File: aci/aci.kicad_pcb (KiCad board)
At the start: 2 copper layers, 102.2 x 53.3 mm, 0 parts

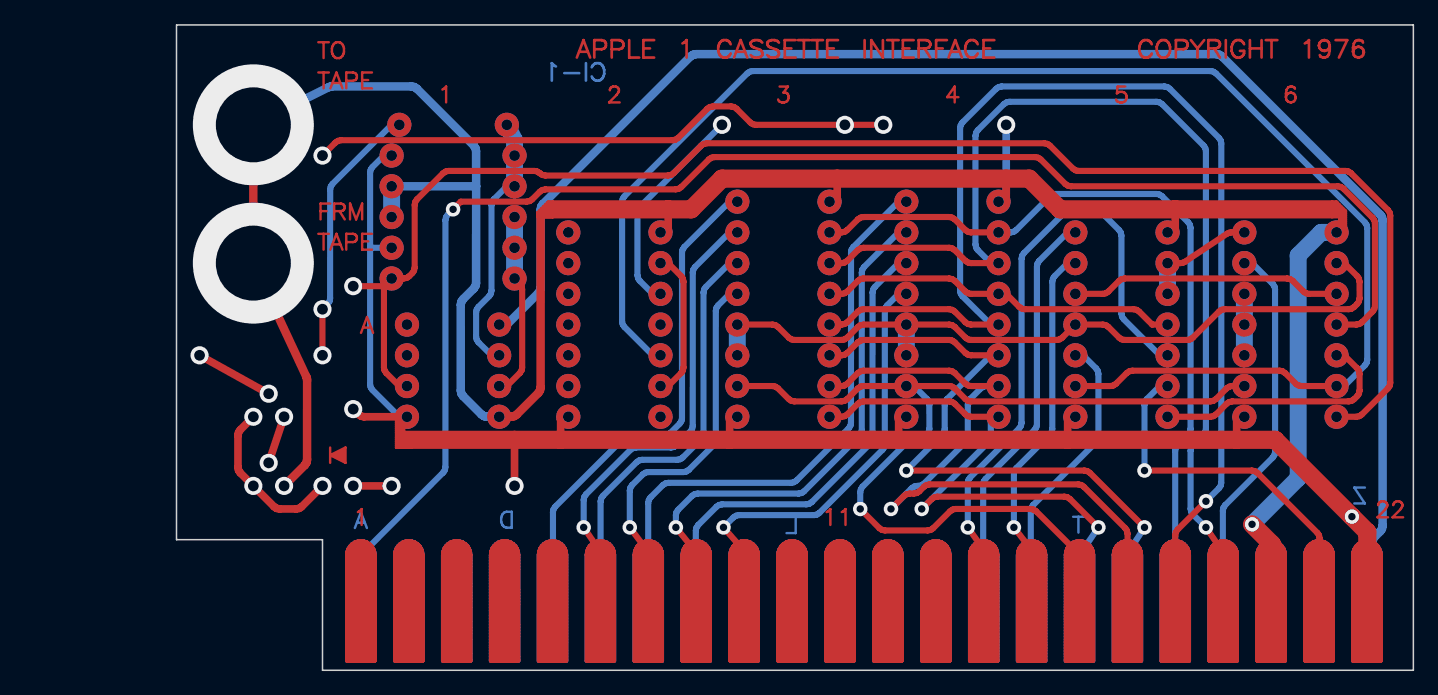
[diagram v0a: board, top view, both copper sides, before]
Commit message: new file:   aci/README.md modified:   aci/aci.kicad_pcb new file:   aci/aci.kicad_pro modified:   aci/aci.kicad_sch deleted:    aci/aci.pro deleted:    aci/aci.sch new file:   doc/apple1cassette.pdf deleted:    doc/progress3d.png
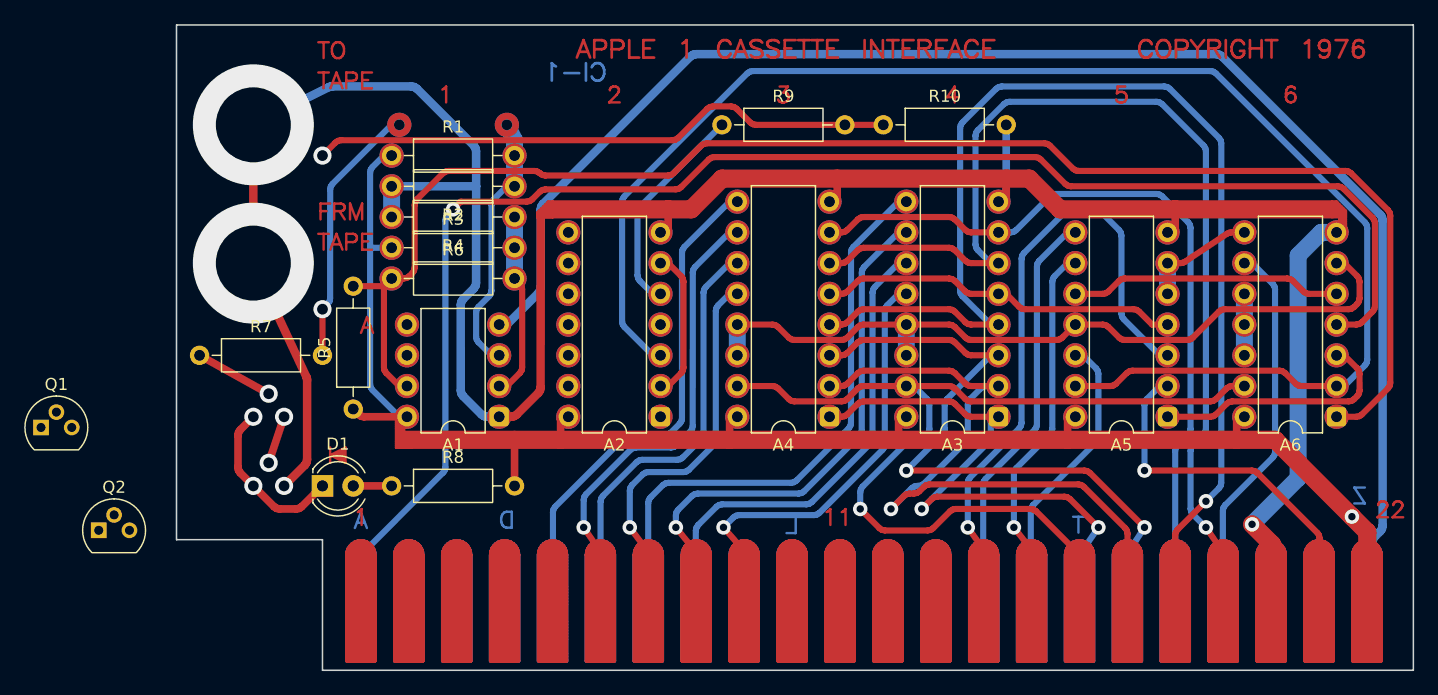
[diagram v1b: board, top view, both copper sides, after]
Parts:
- added A1: LM311, Package_DIP:DIP-8_W7.62mm, F.Cu at (36.8, -31.1)
- added A2: 74LS74, Package_DIP:DIP-14_W7.62mm, F.Cu at (50.2, -31.1)
- added A3: 82S129, Package_DIP:DIP-16_W7.62mm, F.Cu at (78.1, -31.1)
- added A4: 82S129, Package_DIP:DIP-16_W7.62mm, F.Cu at (64.1, -31.1)
- added A5: 74LS02, Package_DIP:DIP-14_W7.62mm, F.Cu at (92.1, -31.1)
- added A6: 74LS10, Package_DIP:DIP-14_W7.62mm, F.Cu at (106.0, -31.1)
- added D1: LED_Small_ALT, LED_THT:LED_D4.0mm, F.Cu at (22.2, -25.4)
- added Q1: Q_NPN_EBC, Package_TO_SOT_THT:TO-92, F.Cu at (-1.04, -30.2)
- added Q2: Q_NPN_EBC, Package_TO_SOT_THT:TO-92, F.Cu at (3.73, -21.7)
- added R1: 10k, Resistor_THT:R_Axial_DIN0207_L6.3mm_D2.5mm_P10.16mm_Horizontal, F.Cu at (27.9, -52.7)
- added R10: 100, Resistor_THT:R_Axial_DIN0207_L6.3mm_D2.5mm_P10.16mm_Horizontal, F.Cu at (68.6, -55.2)
- added R2: 10k, Resistor_THT:R_Axial_DIN0207_L6.3mm_D2.5mm_P10.16mm_Horizontal, F.Cu at (38.1, -50.2)
- added R3: 10k, Resistor_THT:R_Axial_DIN0207_L6.3mm_D2.5mm_P10.16mm_Horizontal, F.Cu at (27.9, -45.1)
- added R4: 10k, Resistor_THT:R_Axial_DIN0207_L6.3mm_D2.5mm_P10.16mm_Horizontal, F.Cu at (38.1, -47.6)
- added R5: 3k, Resistor_THT:R_Axial_DIN0207_L6.3mm_D2.5mm_P10.16mm_Horizontal, F.Cu at (24.8, -31.8)
- added R6: 47k, Resistor_THT:R_Axial_DIN0207_L6.3mm_D2.5mm_P10.16mm_Horizontal, F.Cu at (27.9, -42.5)
- added R7: 100k, Resistor_THT:R_Axial_DIN0207_L6.3mm_D2.5mm_P10.16mm_Horizontal, F.Cu at (12.1, -36.2)
- added R8: 100, Resistor_THT:R_Axial_DIN0207_L6.3mm_D2.5mm_P10.16mm_Horizontal, F.Cu at (27.9, -25.4)
- added R9: 10k, Resistor_THT:R_Axial_DIN0207_L6.3mm_D2.5mm_P10.16mm_Horizontal, F.Cu at (55.2, -55.2)
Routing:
- net 0: track 11525.1 -> 0.00 mm
- net (no net): track 0.00 -> 4125.1 mm, vias 134 -> 8
- net GND: track 0.00 -> 458.4 mm, vias 0 -> 13
- net +5V: track 0.00 -> 362.7 mm, vias 0 -> 11
- net Net-(J3A-ɸ2): track 0.00 -> 332.7 mm, vias 0 -> 2
- net -12V: track 0.00 -> 330.3 mm, vias 0 -> 1
- net Net-(A3-A3): track 0.00 -> 303.6 mm, vias 0 -> 3
- net Net-(A3-A1): track 0.00 -> 293.6 mm, vias 0 -> 3
- net Net-(A3-A7): track 0.00 -> 289.1 mm, vias 0 -> 4
- net Net-(A3-A2): track 0.00 -> 270.9 mm, vias 0 -> 2
- net Net-(A3-A5): track 0.00 -> 263.7 mm, vias 0 -> 3
- net Net-(A3-A4): track 0.00 -> 262.3 mm, vias 0 -> 4
- net Net-(J3A-A11): track 0.00 -> 259.8 mm, vias 0 -> 2
- net Net-(A3-O4): track 0.00 -> 254.8 mm, vias 0 -> 1
- net Net-(A3-A6): track 0.00 -> 254.4 mm, vias 0 -> 4
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
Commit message: modified:   aci/README.md 	modified:   aci/aci.kicad_pcb 	modified:   aci/aci.kicad_sch 	new file:   aci/aci.pretty/aci_TO-92_bent.kicad_mod 	new file:   aci/fp-lib-table 	new file:   doc/aci-assembly-v0.18.pdf 	modified:   mainboard/mainboard.kicad_pcb 	modified:   mainboard/mainboard.kicad_pro
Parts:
- Q1, Q2: footprint Package_TO_SOT_THT:TO-92 -> aci:aci_TO-92_bent
- moved Q1 20.1 mm to (19.1, -31.1), turned to 180 degrees
- moved Q2 15.8 mm to (19.1, -25.4), turned to 180 degrees
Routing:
- net Net-(Q1-E): track 0.00 -> 4.02 mm
- net (no net): track 4125.1 -> 4121.1 mm, vias 8 -> 6
- net Net-(D1-K): vias 3 -> 1
- net Net-(Q1-B): vias 2 -> 1
- net GND: vias 13 -> 12
